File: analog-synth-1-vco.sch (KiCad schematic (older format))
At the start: 13 parts, among them U2 TL084

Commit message: Annotate components
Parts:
- gave numbers to parts that had none: 12
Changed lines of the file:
@@
 $EndComp
 $Comp
-L Device:R R?
+L Device:R R11
 U 1 1 5C8B131B
 P 4100 3400
-F 0 "R?" V 3893 3400 50  0000 C CNN
+F 0 "R11" V 3893 3400 50  0000 C CNN
 F 1 "100k" V 3984 3400 50  0000 C CNN
 F 2 "" V 4030 3400 50  0001 C CNN
@@
 $EndComp
 $Comp
-L Device:R R?
+L Device:R R12
 U 1 1 5C8B1360
 P 4100 3800
-F 0 "R?" V 3893 3800 50  0000 C CNN
+F 0 "R12" V 3893 3800 50  0000 C CNN
 F 1 "50k" V 3984 3800 50  0000 C CNN
 F 2 "" V 4030 3800 50  0001 C CNN
@@
 	3850 3600 3850 3800
 $Comp
-L Device:R R?
+L Device:R R13
 U 1 1 5C8B15F3
 P 4350 4100
-F 0 "R?" H 4420 4146 50  0000 L CNN
+F 0 "R13" H 4420 4146 50  0000 L CNN
 F 1 "50k" H 4420 4055 50  0000 L CNN
 F 2 "" V 4280 4100 50  0001 C CNN
@@
 $EndComp
 $Comp
-L Device:R R?
+L Device:R R14
 U 1 1 5C8B1661
 P 4850 4100
-F 0 "R?" H 4920 4146 50  0000 L CNN
+F 0 "R14" H 4920 4146 50  0000 L CNN
 F 1 "50k" H 4920 4055 50  0000 L CNN
 F 2 "" V 4780 4100 50  0001 C CNN
@@
 	4850 3500 4950 3500
 $Comp
-L Device:C C?
+L Device:C C8
 U 1 1 5C8B17FA
 P 5250 2900
-F 0 "C?" V 4998 2900 50  0000 C CNN
+F 0 "C8" V 4998 2900 50  0000 C CNN
 F 1 "4nf" V 5089 2900 50  0000 C CNN
 F 2 "" H 5288 2750 50  0001 C CNN
@@
 	5650 3600 5550 3600
 $Comp
-L Transistor_BJT:2N3904 Q?
+L Transistor_BJT:2N3904 Q5
 U 1 1 5C8B1AB1
 P 4950 4650
-F 0 "Q?" H 5141 4696 50  0000 L CNN
+F 0 "Q5" H 5141 4696 50  0000 L CNN
 F 1 "2N3904" H 5141 4605 50  0000 L CNN
 F 2 "Package_TO_SOT_THT:TO-92_Inline" H 5150 4575 50  0001 L CIN
@@
 	4850 4250 4850 4450
 $Comp
-L power:GND #PWR?
+L power:GND #PWR028
 U 1 1 5C8B1C4F
 P 4600 5050
-F 0 "#PWR?" H 4600 4800 50  0001 C CNN
+F 0 "#PWR028" H 4600 4800 50  0001 C CNN
 F 1 "GND" H 4605 4877 50  0000 C CNN
 F 2 "" H 4600 5050 50  0001 C CNN
@@
 Connection ~ 4600 4950
 $Comp
-L Transistor_BJT:2N3906 Q?
+L Transistor_BJT:2N3906 Q6
 U 1 1 5C8B214B
 P 5550 4750
-F 0 "Q?" V 5878 4750 50  0000 C CNN
+F 0 "Q6" V 5878 4750 50  0000 C CNN
 F 1 "2N3906" V 5787 4750 50  0000 C CNN
 F 2 "Package_TO_SOT_THT:TO-92_Inline" H 5750 4675 50  0001 L CIN
@@
 Connection ~ 5650 3600
 $Comp
-L Device:R R?
+L Device:R R15
 U 1 1 5C8B2DE4
 P 5850 3400
-F 0 "R?" H 5920 3446 50  0000 L CNN
+F 0 "R15" H 5920 3446 50  0000 L CNN
 F 1 "100k" H 5920 3355 50  0000 L CNN
 F 2 "" V 5780 3400 50  0001 C CNN
@@
 $EndComp
 $Comp
-L power:+5V #PWR?
+L power:+5V #PWR029
 U 1 1 5C8B2E30
 P 5850 3200
-F 0 "#PWR?" H 5850 3050 50  0001 C CNN
+F 0 "#PWR029" H 5850 3050 50  0001 C CNN
 F 1 "+5V" H 5865 3373 50  0000 C CNN
 F 2 "" H 5850 3200 50  0001 C CNN
@@
 	5850 3200 5850 3250
 $Comp
-L Device:R R?
+L Device:R R17
 U 1 1 5C8B34C8
 P 6100 3900
-F 0 "R?" V 5893 3900 50  0000 C CNN
+F 0 "R17" V 5893 3900 50  0000 C CNN
 F 1 "50k" V 5984 3900 50  0000 C CNN
 F 2 "" V 6030 3900 50  0001 C CNN
@@
 	6350 3800 6300 3800
 $Comp
-L Device:R R?
+L Device:R R16
 U 1 1 5C8B3D38
 P 5850 4100
-F 0 "R?" H 5920 4146 50  0000 L CNN
+F 0 "R16" H 5920 4146 50  0000 L CNN
 F 1 "100k" H 5920 4055 50  0000 L CNN
 F 2 "" V 5780 4100 50  0001 C CNN
@@
 $EndComp
 $Comp
-L power:GND #PWR?
+L power:GND #PWR030
 U 1 1 5C8B3D96
 P 5850 4300
-F 0 "#PWR?" H 5850 4050 50  0001 C CNN
+F 0 "#PWR030" H 5850 4050 50  0001 C CNN
 F 1 "GND" H 5855 4127 50  0000 C CNN
 F 2 "" H 5850 4300 50  0001 C CNN
@@
 Connection ~ 5850 3900
 $Comp
-L Device:R R?
+L Device:R R18
 U 1 1 5C8B5A3B
 P 6650 4200
-F 0 "R?" V 6857 4200 50  0000 C CNN
+F 0 "R18" V 6857 4200 50  0000 C CNN
 F 1 "100k" V 6766 4200 50  0000 C CNN
 F 2 "" V 6580 4200 50  0001 C CNN
@@
 Connection ~ 7050 3700
 $Comp
-L Device:R R?
+L Device:R R19
 U 1 1 5C8B6C57
 P 6650 4650
-F 0 "R?" V 6443 4650 50  0000 C CNN
+F 0 "R19" V 6443 4650 50  0000 C CNN
 F 1 "100k" V 6534 4650 50  0000 C CNN
 F 2 "" V 6580 4650 50  0001 C CNN

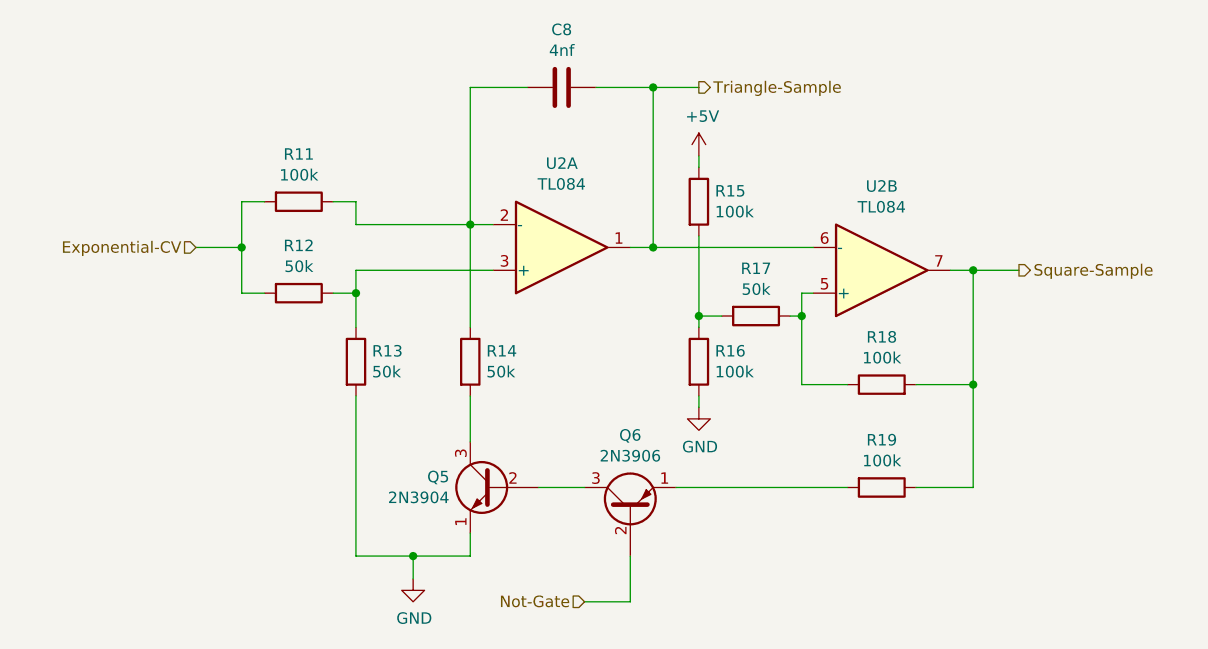
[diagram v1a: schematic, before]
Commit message: Add ATtiny85 overdrive protection, fix #5
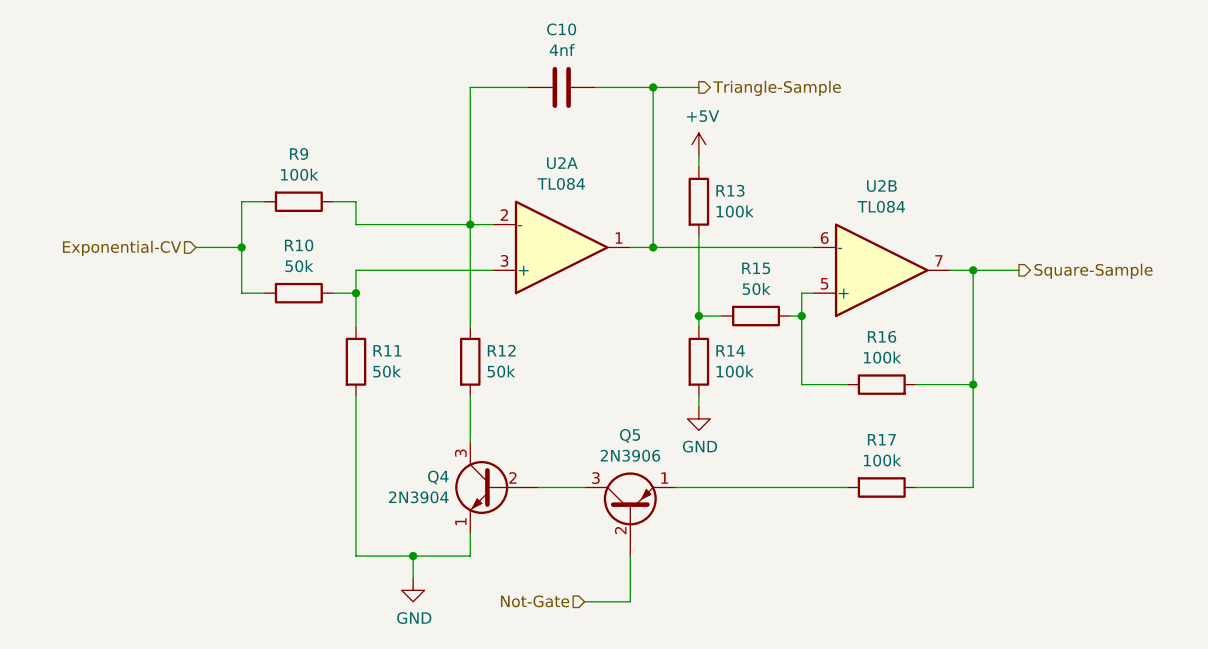
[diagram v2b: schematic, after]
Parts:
- renumbered C8 to C10, Q5 to Q4, Q6 to Q5, R12 to R10, R13 to R11, R14 to R12, R15 to R13, R16 to R14, R17 to R15, R18 to R16, R19 to R17, R11 to R9
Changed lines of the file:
@@
 $EndComp
 $Comp
-L Device:R R11
+L Device:R R9
 U 1 1 5C8B131B
 P 4100 3400
-F 0 "R11" V 3893 3400 50  0000 C CNN
+F 0 "R9" V 3893 3400 50  0000 C CNN
 F 1 "100k" V 3984 3400 50  0000 C CNN
 F 2 "" V 4030 3400 50  0001 C CNN
@@
 $EndComp
 $Comp
-L Device:R R12
+L Device:R R10
 U 1 1 5C8B1360
 P 4100 3800
-F 0 "R12" V 3893 3800 50  0000 C CNN
+F 0 "R10" V 3893 3800 50  0000 C CNN
 F 1 "50k" V 3984 3800 50  0000 C CNN
 F 2 "" V 4030 3800 50  0001 C CNN
@@
 	3850 3600 3850 3800
 $Comp
-L Device:R R13
+L Device:R R11
 U 1 1 5C8B15F3
 P 4350 4100
-F 0 "R13" H 4420 4146 50  0000 L CNN
+F 0 "R11" H 4420 4146 50  0000 L CNN
 F 1 "50k" H 4420 4055 50  0000 L CNN
 F 2 "" V 4280 4100 50  0001 C CNN
@@
 $EndComp
 $Comp
-L Device:R R14
+L Device:R R12
 U 1 1 5C8B1661
 P 4850 4100
-F 0 "R14" H 4920 4146 50  0000 L CNN
+F 0 "R12" H 4920 4146 50  0000 L CNN
 F 1 "50k" H 4920 4055 50  0000 L CNN
 F 2 "" V 4780 4100 50  0001 C CNN
@@
 	4850 3500 4950 3500
 $Comp
-L Device:C C8
+L Device:C C10
 U 1 1 5C8B17FA
 P 5250 2900
-F 0 "C8" V 4998 2900 50  0000 C CNN
+F 0 "C10" V 4998 2900 50  0000 C CNN
 F 1 "4nf" V 5089 2900 50  0000 C CNN
 F 2 "" H 5288 2750 50  0001 C CNN
@@
 	5650 3600 5550 3600
 $Comp
-L Transistor_BJT:2N3904 Q5
+L Transistor_BJT:2N3904 Q4
 U 1 1 5C8B1AB1
 P 4950 4650
-F 0 "Q5" H 5141 4696 50  0000 L CNN
+F 0 "Q4" H 5141 4696 50  0000 L CNN
 F 1 "2N3904" H 5141 4605 50  0000 L CNN
 F 2 "Package_TO_SOT_THT:TO-92_Inline" H 5150 4575 50  0001 L CIN
@@
 	4850 4250 4850 4450
 $Comp
-L power:GND #PWR028
+L power:GND #PWR031
 U 1 1 5C8B1C4F
 P 4600 5050
-F 0 "#PWR028" H 4600 4800 50  0001 C CNN
+F 0 "#PWR031" H 4600 4800 50  0001 C CNN
 F 1 "GND" H 4605 4877 50  0000 C CNN
 F 2 "" H 4600 5050 50  0001 C CNN
@@
 Connection ~ 4600 4950
 $Comp
-L Transistor_BJT:2N3906 Q6
+L Transistor_BJT:2N3906 Q5
 U 1 1 5C8B214B
 P 5550 4750
-F 0 "Q6" V 5878 4750 50  0000 C CNN
+F 0 "Q5" V 5878 4750 50  0000 C CNN
 F 1 "2N3906" V 5787 4750 50  0000 C CNN
 F 2 "Package_TO_SOT_THT:TO-92_Inline" H 5750 4675 50  0001 L CIN
@@
 Connection ~ 5650 3600
 $Comp
-L Device:R R15
+L Device:R R13
 U 1 1 5C8B2DE4
 P 5850 3400
-F 0 "R15" H 5920 3446 50  0000 L CNN
+F 0 "R13" H 5920 3446 50  0000 L CNN
 F 1 "100k" H 5920 3355 50  0000 L CNN
 F 2 "" V 5780 3400 50  0001 C CNN
@@
 $EndComp
 $Comp
-L power:+5V #PWR029
+L power:+5V #PWR032
 U 1 1 5C8B2E30
 P 5850 3200
-F 0 "#PWR029" H 5850 3050 50  0001 C CNN
+F 0 "#PWR032" H 5850 3050 50  0001 C CNN
 F 1 "+5V" H 5865 3373 50  0000 C CNN
 F 2 "" H 5850 3200 50  0001 C CNN
@@
 	5850 3200 5850 3250
 $Comp
-L Device:R R17
+L Device:R R15
 U 1 1 5C8B34C8
 P 6100 3900
-F 0 "R17" V 5893 3900 50  0000 C CNN
+F 0 "R15" V 5893 3900 50  0000 C CNN
 F 1 "50k" V 5984 3900 50  0000 C CNN
 F 2 "" V 6030 3900 50  0001 C CNN
@@
 	6350 3800 6300 3800
 $Comp
-L Device:R R16
+L Device:R R14
 U 1 1 5C8B3D38
 P 5850 4100
-F 0 "R16" H 5920 4146 50  0000 L CNN
+F 0 "R14" H 5920 4146 50  0000 L CNN
 F 1 "100k" H 5920 4055 50  0000 L CNN
 F 2 "" V 5780 4100 50  0001 C CNN
@@
 $EndComp
 $Comp
-L power:GND #PWR030
+L power:GND #PWR033
 U 1 1 5C8B3D96
 P 5850 4300
-F 0 "#PWR030" H 5850 4050 50  0001 C CNN
+F 0 "#PWR033" H 5850 4050 50  0001 C CNN
 F 1 "GND" H 5855 4127 50  0000 C CNN
 F 2 "" H 5850 4300 50  0001 C CNN
@@
 Connection ~ 5850 3900
 $Comp
-L Device:R R18
+L Device:R R16
 U 1 1 5C8B5A3B
 P 6650 4200
-F 0 "R18" V 6857 4200 50  0000 C CNN
+F 0 "R16" V 6857 4200 50  0000 C CNN
 F 1 "100k" V 6766 4200 50  0000 C CNN
 F 2 "" V 6580 4200 50  0001 C CNN
@@
 Connection ~ 7050 3700
 $Comp
-L Device:R R19
+L Device:R R17
 U 1 1 5C8B6C57
 P 6650 4650
-F 0 "R19" V 6443 4650 50  0000 C CNN
+F 0 "R17" V 6443 4650 50  0000 C CNN
 F 1 "100k" V 6534 4650 50  0000 C CNN
 F 2 "" V 6580 4650 50  0001 C CNN
